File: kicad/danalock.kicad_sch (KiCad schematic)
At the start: 11 parts, among them J1 Conn_01x02, J2 Conn_01x07, J3 Conn_01x03, U1 ESP32mini_shield_inner, U2 DSN-MINI-360

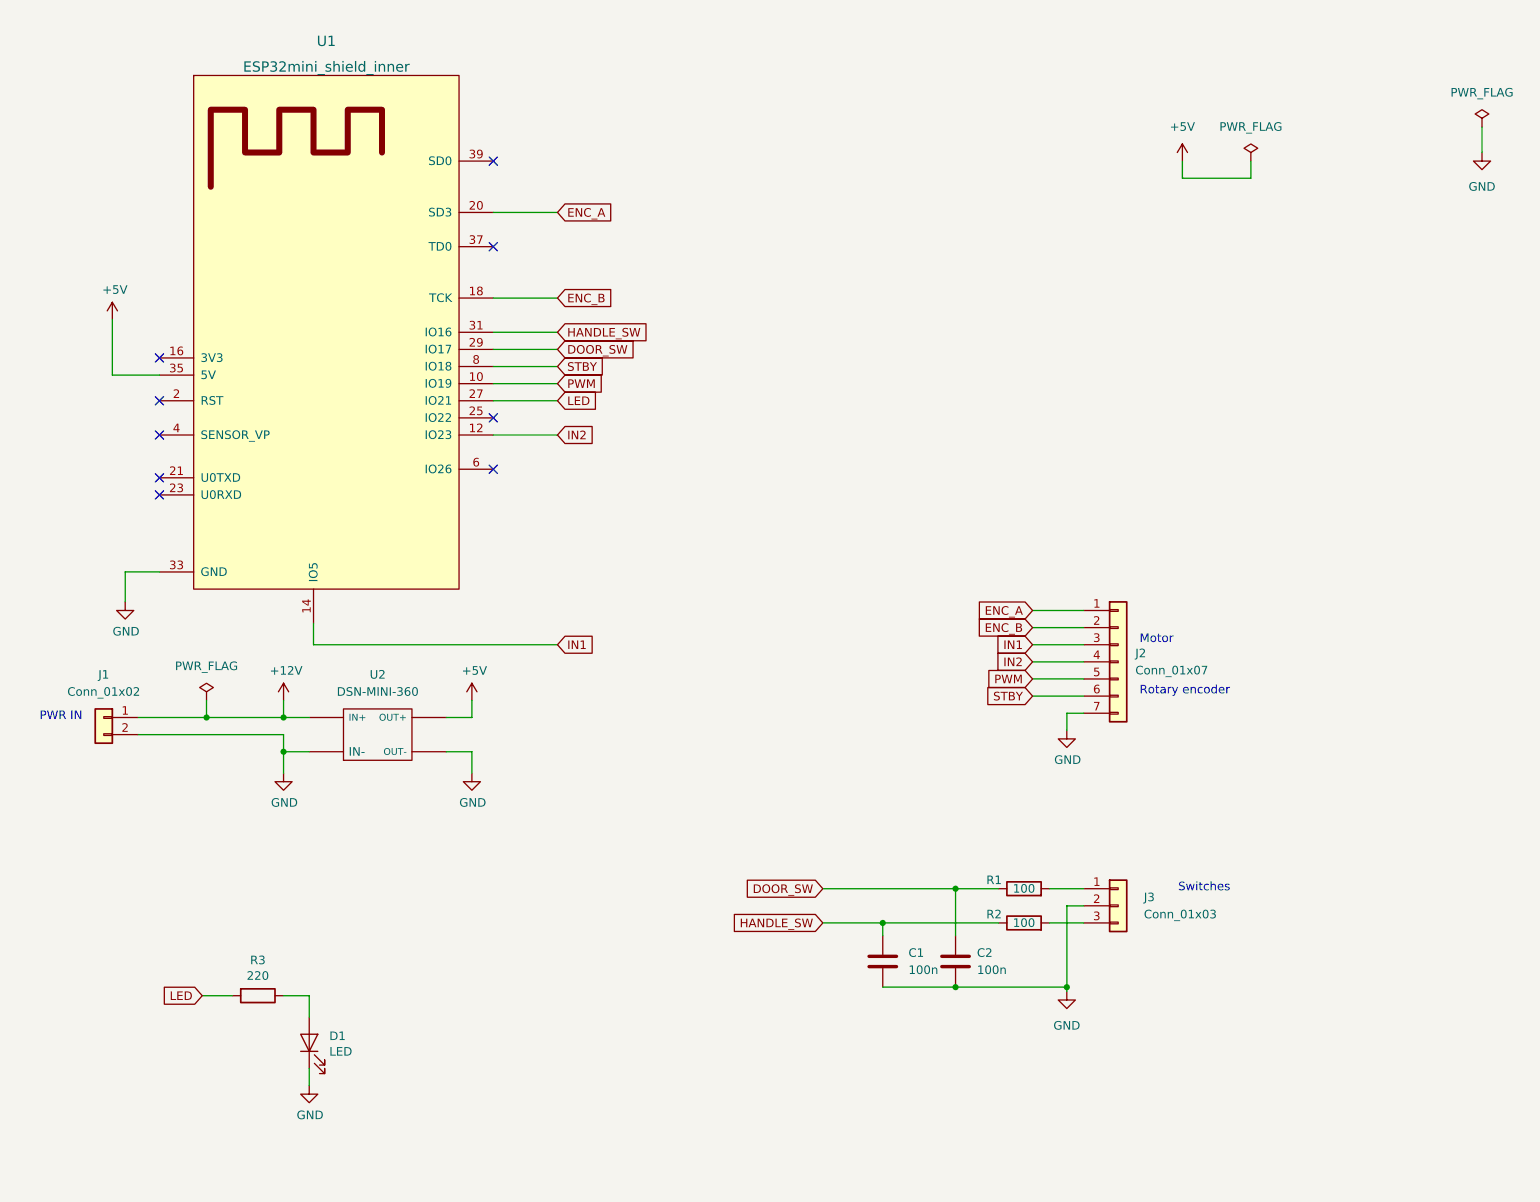
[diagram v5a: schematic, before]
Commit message: Fix orientation, add missing 3V3 pin.
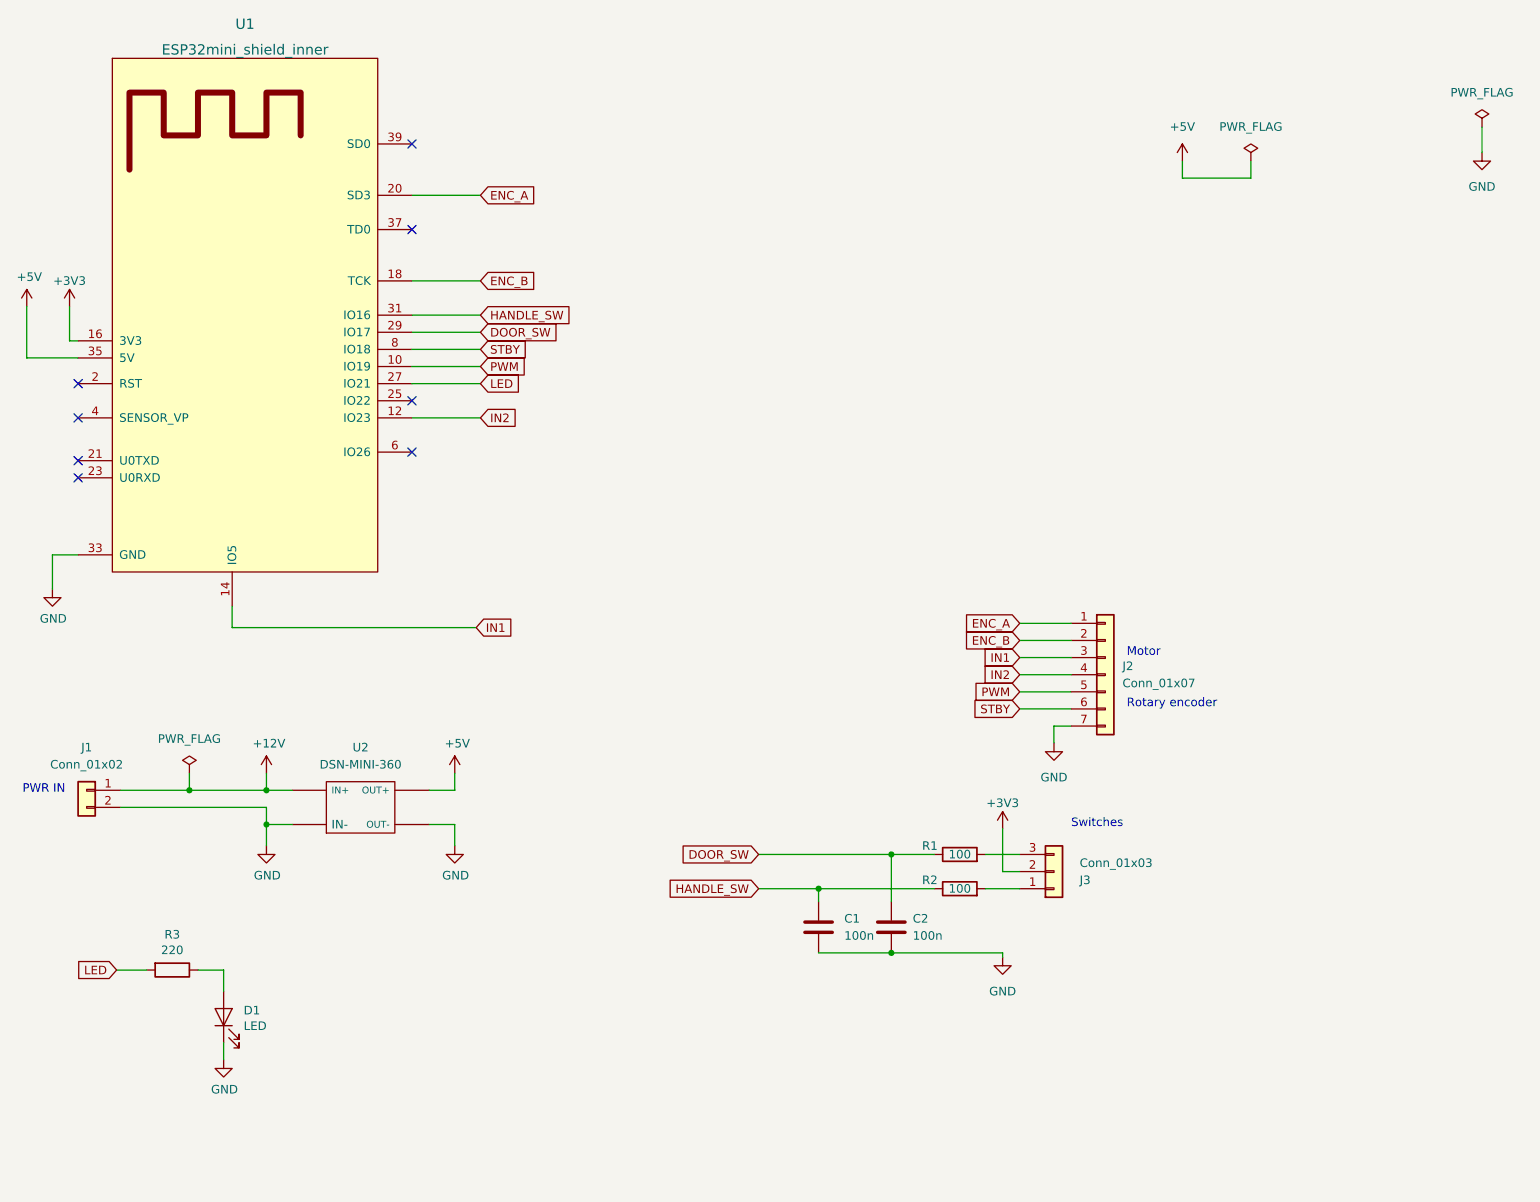
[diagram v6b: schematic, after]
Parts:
- D1: footprint LED_THT:LED_D5.0mm -> LED_THT:LED_D5.0mm_Clear
- J2: footprint Connector_PinSocket_2.00mm:PinSocket_1x07_P2.00mm_Vertical -> Connector_PinHeader_2.00mm:PinHeader_1x07_P2.00mm_Vertical
- J3: footprint Connector_PinSocket_2.00mm:PinSocket_1x03_P2.00mm_Vertical -> Connector_PinHeader_2.00mm:PinHeader_1x03_P2.00mm_Vertical
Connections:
- net GND: no longer J3.2 (Pin_2)
- net at J3.1 (Pin_1): now also R2.2; no longer R1.2
- net at J3.3 (Pin_3): now also R1.2; no longer R2.2
- net +3V3: now reaches U1.16 (3V3)
- net +3V3: now also J3.2 (Pin_2)
- no-connect marks 9 -> 8
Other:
- moved on the sheet: C1, C2, D1, J1, J2, J3, R1, R2, R3, U1, U2

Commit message: Fix footprints.
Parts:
- D1: footprint LED_THT:LED_D5.0mm_Clear -> LED_THT:LED_Rectangular_W5.0mm_H2.0mm
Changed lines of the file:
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@@
       (effects (font (size 1.27 1.27)) (justify right))
     )
-    (property "Footprint" "LED_THT:LED_D5.0mm_Clear" (at 62.23 163.83 0)
+    (property "Footprint" "LED_THT:LED_Rectangular_W5.0mm_H2.0mm" (at 62.23 163.83 0)
       (effects (font (size 1.27 1.27)) hide)
     )
